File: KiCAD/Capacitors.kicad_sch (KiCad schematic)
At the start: 50 parts, among them U11 74LS367

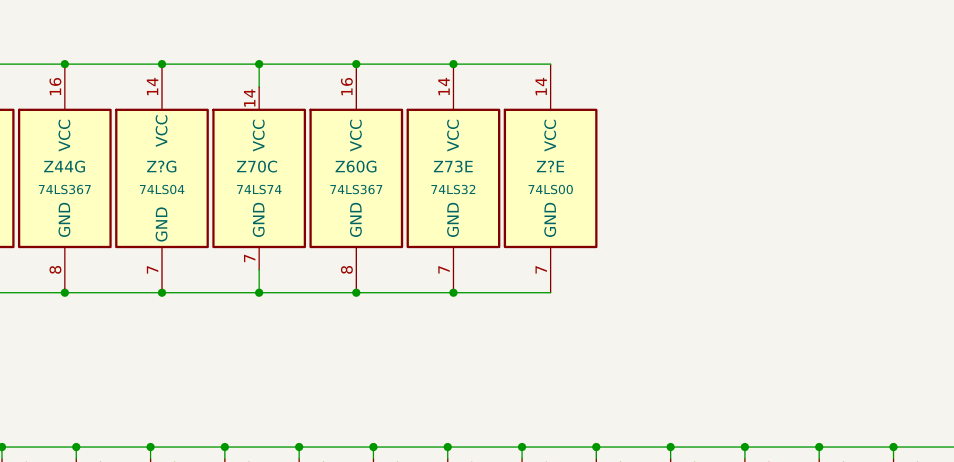
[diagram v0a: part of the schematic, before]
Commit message: Update schematics (correct page flow) and add alternative to Q4 in BOM
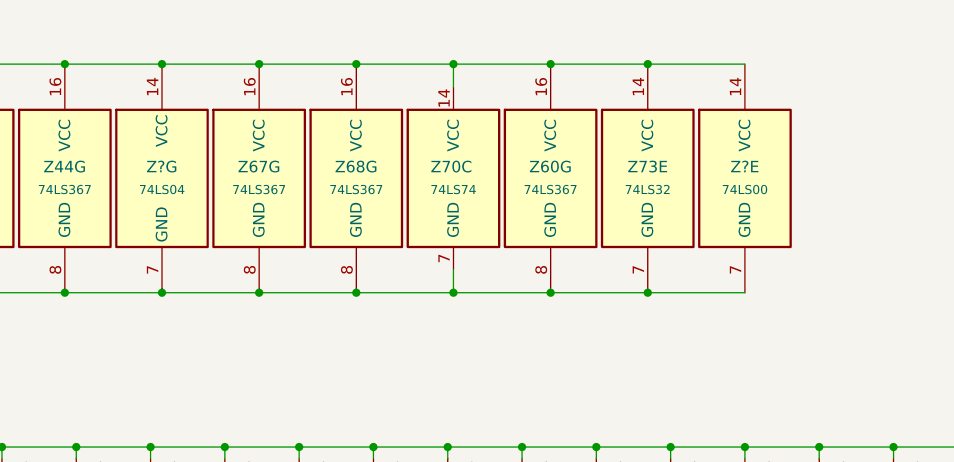
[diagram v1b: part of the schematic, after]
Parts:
- added Z67, Z68: 74LS367, RetroStackLibrary:TRS80_Model_I_DIP16, symbol RetroStackLibrary:74LS367_Split
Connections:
- net +5V: now also Z67.16 (VCC), Z68.16 (VCC)
- net GND: now also Z67.8 (GND), Z68.8 (GND)
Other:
- moved on the sheet: Z60G, Z70C, Z73E, Z?E

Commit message: Updated revision to Rev C
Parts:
- gave numbers to parts that had none: 5
- renumbered Z37 to Z30, U11 to Z72
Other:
- title: TRS-80 Model I G -> TRS-80 Model I Rev G
